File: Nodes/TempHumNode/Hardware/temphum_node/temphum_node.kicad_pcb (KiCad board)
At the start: 2 copper layers, 63.5 x 51.3 mm, 37 parts, among them IC1 CC1310F128RGZR, IC2 TPD6E004RSER, J1 TC2050-IDC, U1 MCP73123-22SI/MF, Y2 TSX-3225 24.0000MF15X-AC3, Y3 FC-135_32.7680KA-AG0

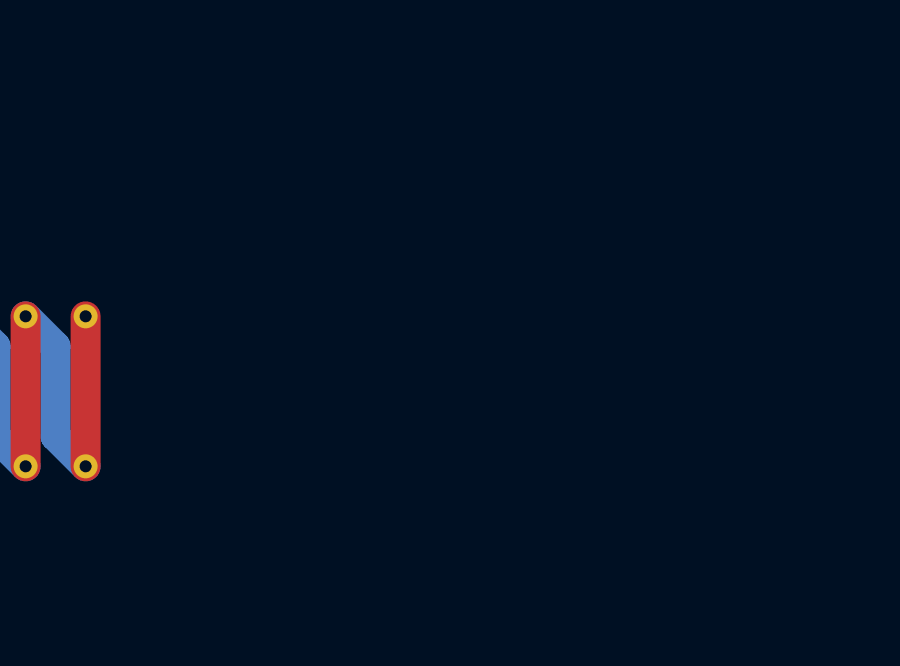
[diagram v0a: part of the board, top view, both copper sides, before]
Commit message: hw(temphum-node): add SHT35 (custom symbol layout) + schematic/board progress
Import SHT35-DIS-B (LCSC C90161) footprint + 3D model, and swap the
symbol graphics for the user's custom pin arrangement from the
temperatureSensorSubGHz project (keeps footprint link + LCSC/BOM
fields). Plus in-progress schematic/board work.

Co-Authored-By: Claude Opus 4.8 (1M context) <noreply@anthropic.com>
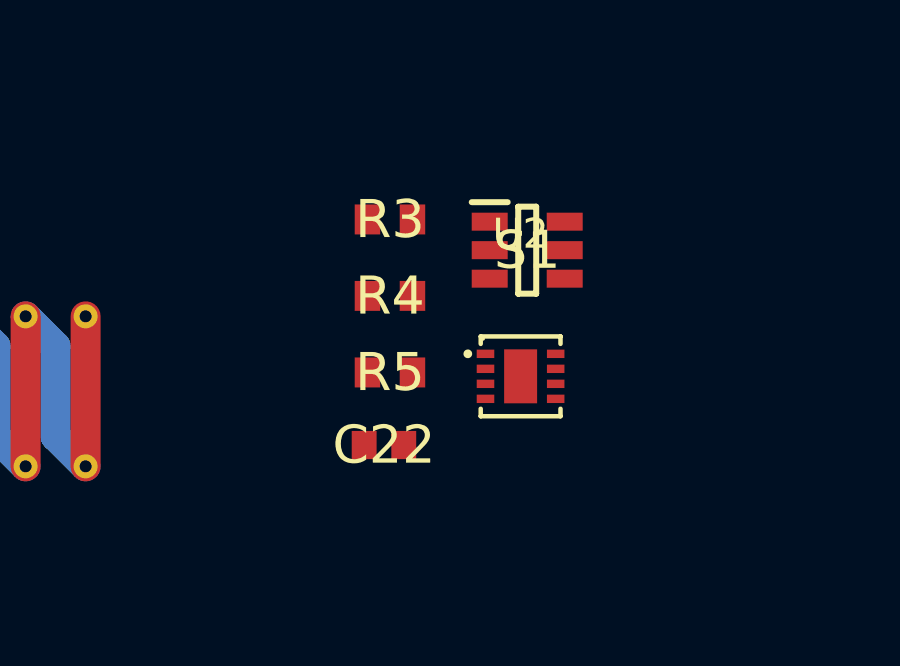
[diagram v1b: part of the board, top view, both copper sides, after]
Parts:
- added C22: 100nF, CC0603KRX7R9BB104:CAPC1608X90N, F.Cu at (179.3, 35.6)
- added R3: 10k, CRCW060310K0FKEA:RESC1608X50N, F.Cu at (179.5, 28.1)
- added R4: 10k, CRCW060310K0FKEA:RESC1608X50N, F.Cu at (179.5, 30.7)
- added R5: 10k, CRCW060310K0FKEA:RESC1608X50N, F.Cu at (179.5, 33.2)
- added S1: TPS22860DBVR, TPS22860DBVR:SOT95P280X145-6N, F.Cu at (184.1, 29.1)
- added U2: SHT35-DIS-B, SmartHome:DFN-8_L2.5-W2.5-P0.50-TL-EP, F.Cu at (183.9, 33.3)

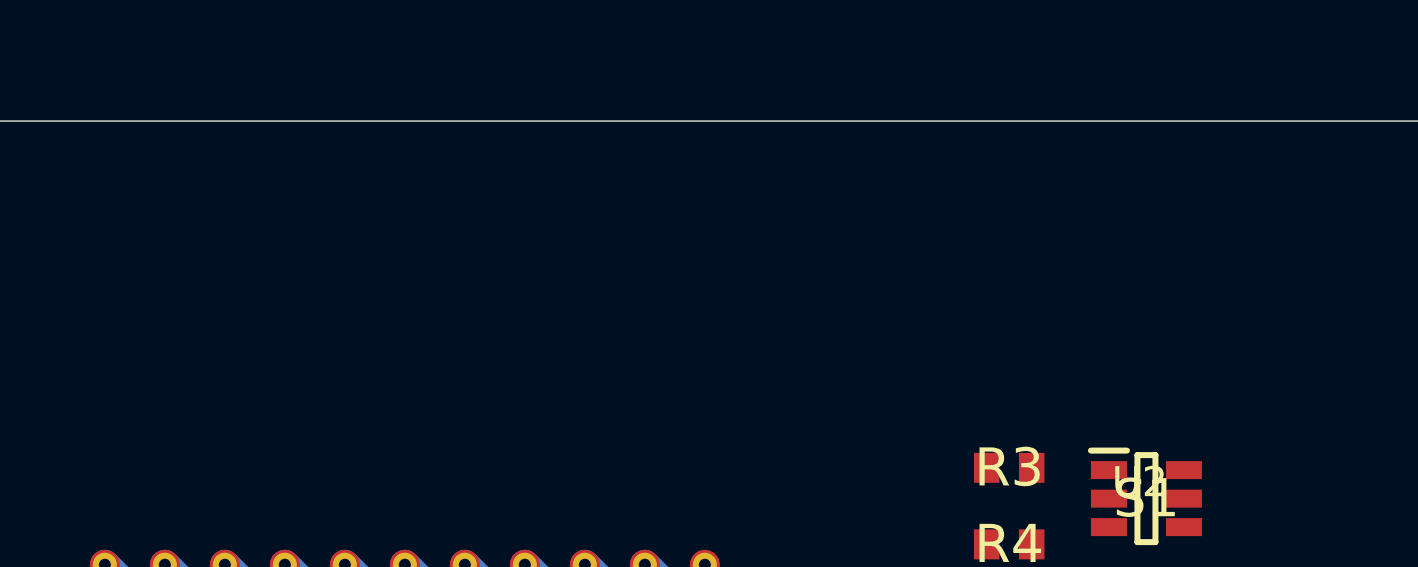
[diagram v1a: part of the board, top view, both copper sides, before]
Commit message: hw(temphum-node): add power/protection parts (TPS63900, MCP3421, TPS22860, PCM)
Import LDO/converter TPS63900 (buck-boost 3.3V), MCP3421A0 (18-bit ADC,
I2C 0x68 for battery SoC), TPS22860 (load switch), and the LiFePO4 PCM
pair HY2112 + FS8205A. Footprints/symbols/3D into Shared/KiCadLib.

Co-Authored-By: Claude Opus 4.8 (1M context) <noreply@anthropic.com>
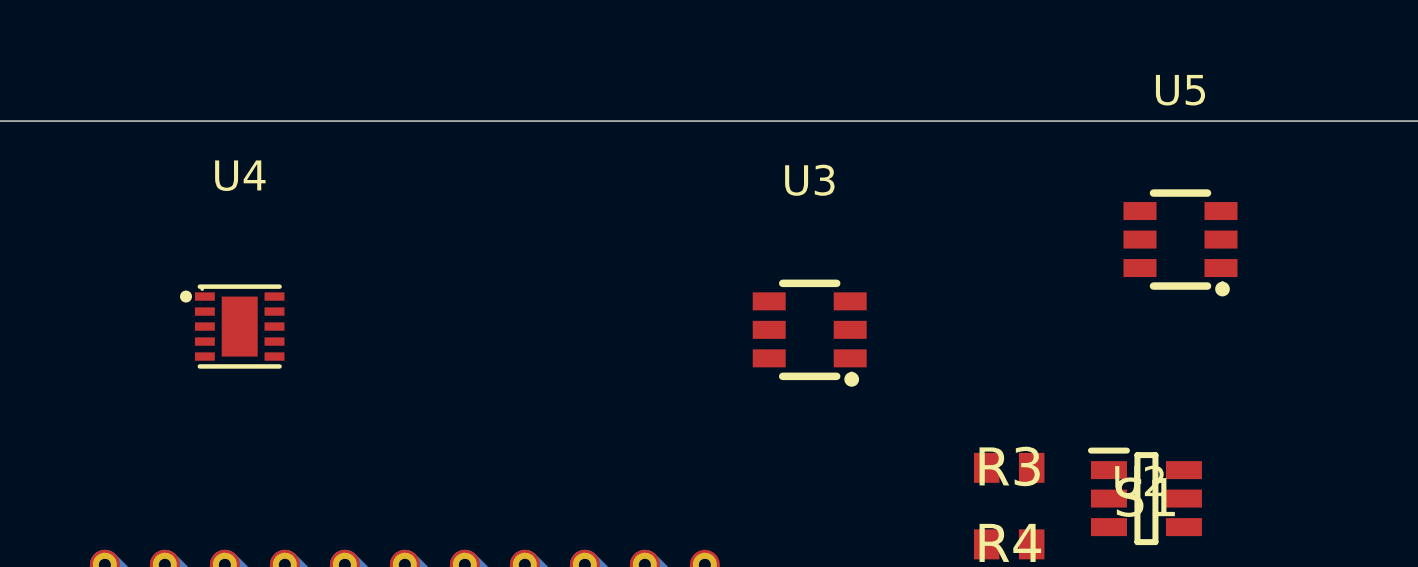
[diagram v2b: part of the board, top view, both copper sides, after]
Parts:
- added U3: TPS22860DBVR, SmartHome:SOT-23-6_L2.9-W1.6-P0.95-LS2.8-BR, F.Cu at (172.9, 23.5)
- added U4: TPS63900DSKR, SmartHome:WSON-10_L2.5-W2.5-W0.50-TL-EP, F.Cu at (153.9, 23.4)
- added U5: MCP3421A0T-E/CH, SmartHome:SOT-23-6_L2.9-W1.6-P0.95-LS2.8-BR, F.Cu at (185.2, 20.5)

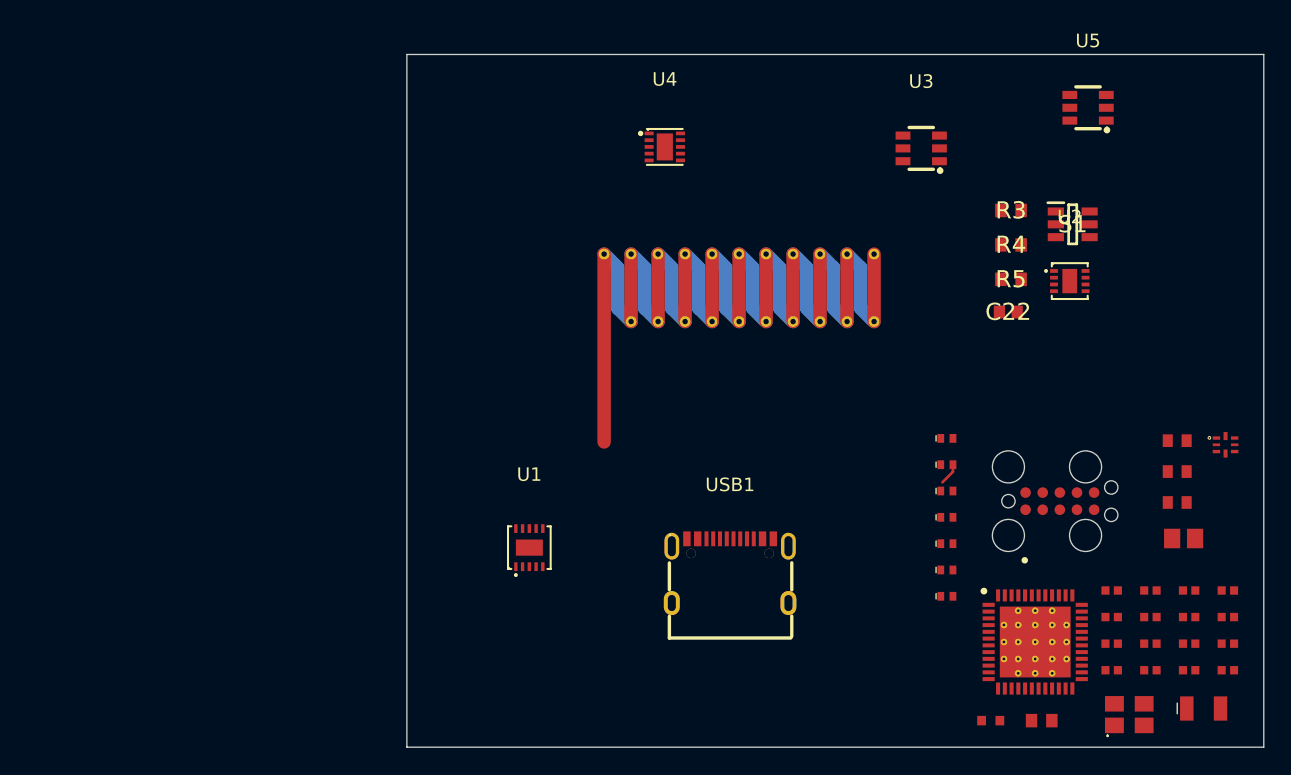
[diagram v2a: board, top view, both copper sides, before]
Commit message: hw(temphum-node): CC1310 support parts - pogo/ESD 3D, crystal swaps
Add TC2030-IDC UART pogo (SnapEDA, both footprints + 3D, symbol made
SmartHome-native). Attach TPD6E004 ESD 3D model + merge its symbol into
SmartHome. Add in-stock crystal replacements: ECS-240-9-33B (24MHz 9pF,
capless HF) and Epson FC-135R (32.768kHz 12.5pF, 2x12pF caps) - both CL/
ESR-matched drop-ins. Plus CC1310 schematic GPIO/pogo wiring.

Co-Authored-By: Claude Opus 4.8 (1M context) <noreply@anthropic.com>
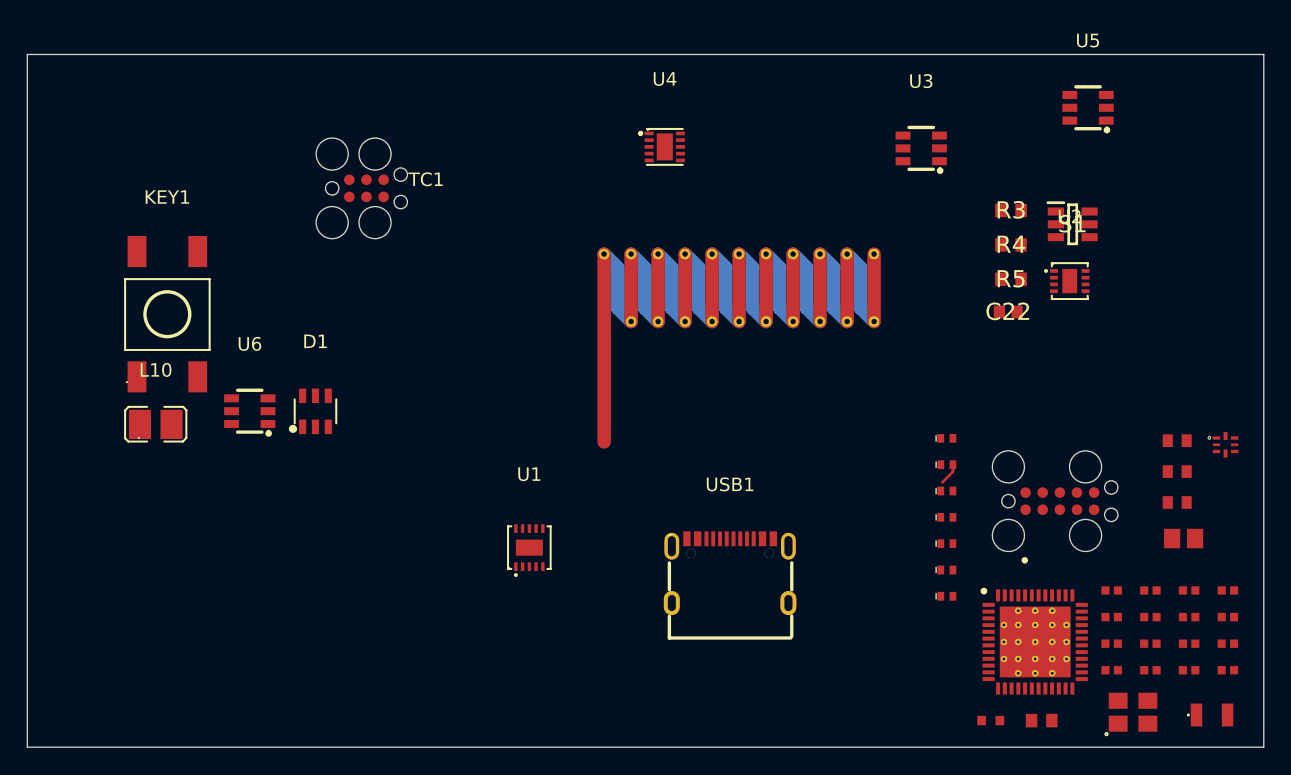
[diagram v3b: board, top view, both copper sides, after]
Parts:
- removed Y2: TSX-3225 24.0000MF15X-AC3, SmartHome:TSX3225240000MF15XAC3
- removed Y3: FC-135_32.7680KA-AG0, SmartHome:FC135327680KAAG0
- added D1: USBLC6-2SC6, SmartHome:SOT-23-6_L2.9-W1.6-P0.95-LS2.8-BL, F.Cu at (128.0, 43.0)
- added KEY1: TL3301AF160QG, SmartHome:KEY-SMD_4P-L6.0-W6.0-P4.50-LS10.0, F.Cu at (117.0, 35.8)
- added L10: DFE252012PD, SmartHome:L1008, F.Cu at (116.2, 44.0)
- added TC1: TC2030-IDC, SmartHome:TC2030-IDC, F.Cu at (131.8, 26.5)
- added U6: TPS22860DBVR, SmartHome:SOT-23-6_L2.9-W1.6-P0.95-LS2.8-BR, F.Cu at (123.1, 43.0)
- added U7: ECS-240-9-33B-CWN-TR, SmartHome:CRYSTAL-SMD_4P-L3.2-W2.5-BL, F.Cu at (188.6, 65.3)
- added X1: FC-135R, SmartHome:OSC-SMD_L3.2-W1.5, F.Cu at (194.4, 65.5)
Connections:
- C22 pad 1: VCC_SWITCH -> 3V3_SW
- IC1 pad 10: unconnected-(IC1-DIO_5-Pad10) -> PERIPH_EN
- IC1 pad 11: unconnected-(IC1-DIO_6-Pad11) -> nBUTTON
- IC1 pad 12: unconnected-(IC1-DIO_7-Pad12) -> nCHRGSTAT
- IC1 pad 37: LED_RED -> unconnected-(IC1-DIO_24-Pad37)
- IC1 pad 38: LED_BLUE -> unconnected-(IC1-DIO_25-Pad38)
- IC1 pad 39: TOUCH_OUT -> unconnected-(IC1-DIO_26-Pad39)
- IC1 pad 40: RELAY1 -> unconnected-(IC1-DIO_27-Pad40)
- IC1 pad 6: unconnected-(IC1-DIO_1-Pad6) -> SCL
- IC1 pad 7: unconnected-(IC1-DIO_2-Pad7) -> SDA
- IC1 pad 8: unconnected-(IC1-DIO_3-Pad8) -> UART_TX
- IC1 pad 9: unconnected-(IC1-DIO_4-Pad9) -> UART_RX
- IC2 pad 7: unconnected-(IC2-IO6-Pad7) -> nBUTTON
- R3 pad 2: VCC_SWITCH -> 3V3_SW
- R4 pad 2: VCC_SWITCH -> 3V3_SW
- R5 pad 2: VCC_SWITCH -> 3V3_SW
- U1 pad 1: unconnected-(U1-VDD-Pad1) -> VBUS
- U1 pad 10: unconnected-(U1-PROG-Pad10) -> Net-(U1-PROG)
- U1 pad 11: unconnected-(U1-EP-Pad11) -> GND
- U1 pad 2: unconnected-(U1-VDD-Pad2) -> VBUS
- U1 pad 3: unconnected-(U1-VBAT-Pad3) -> BAT+
- U1 pad 4: unconnected-(U1-VBAT-Pad4) -> BAT+
- U1 pad 7: unconnected-(U1-STAT-Pad7) -> nCHRGSTAT
- U1 pad 8: unconnected-(U1-VSS-Pad8) -> GND
- U1 pad 9: unconnected-(U1-VSS-Pad9) -> GND
- U2 pad 2: VCC_SWITCH -> 3V3_SW
- U2 pad 5: VCC_SWITCH -> 3V3_SW
- U3 pad 1: VCC_SWITCH -> 3V3_SW
- U3 pad 4: VCC -> 3V3
- U3 pad 5: VCC -> 3V3
- U3 pad 6: DRV_OUT -> PERIPH_EN
- U4 pad 1: unconnected-(U4-EN-Pad1) -> BAT+
- U4 pad 10: unconnected-(U4-VIN-Pad10) -> BAT+
- U4 pad 11: unconnected-(U4-EP-Pad11) -> GND
- U4 pad 2: unconnected-(U4-SEL-Pad2) -> BAT+
- U4 pad 3: unconnected-(U4-CFG1-Pad3) -> Net-(U4-CFG1)
- U4 pad 4: unconnected-(U4-CFG2-Pad4) -> GND
- U4 pad 5: unconnected-(U4-CFG3-Pad5) -> GND
- U4 pad 6: unconnected-(U4-VOUT-Pad6) -> 3V3
- U4 pad 7: unconnected-(U4-LX2-Pad7) -> Net-(U4-LX2)
- U4 pad 8: unconnected-(U4-GND-Pad8) -> GND
- U4 pad 9: unconnected-(U4-LX1-Pad9) -> Net-(U4-LX1)
- U5 pad 1: unconnected-(U5-Vin+-Pad1) -> Net-(U5-Vin+)
- U5 pad 2: unconnected-(U5-VSS-Pad2) -> GND
- U5 pad 3: unconnected-(U5-SCL-Pad3) -> SCL
- U5 pad 4: unconnected-(U5-SDA-Pad4) -> SDA
- U5 pad 5: unconnected-(U5-VDD-Pad5) -> 3V3_SW
- U5 pad 6: unconnected-(U5-Vin--Pad6) -> GND
- USB1 pad 13: unconnected-(USB1-EH-Pad13) -> GND
- USB1 pad 14: unconnected-(USB1-EH-Pad14) -> GND
- USB1 pad A1B12: unconnected-(USB1-GND-PadA1B12) -> GND
- USB1 pad A4B9: unconnected-(USB1-VBUS-PadA4B9) -> VBUS
- USB1 pad A5: unconnected-(USB1-CC1-PadA5) -> CC1
- USB1 pad B1A12: unconnected-(USB1-GND-PadB1A12) -> GND
- USB1 pad B4A9: unconnected-(USB1-VBUS-PadB4A9) -> VBUS
- USB1 pad B5: unconnected-(USB1-CC2-PadB5) -> CC2
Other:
- board size 63.5 x 51.3 mm -> 91.6 x 51.3 mm

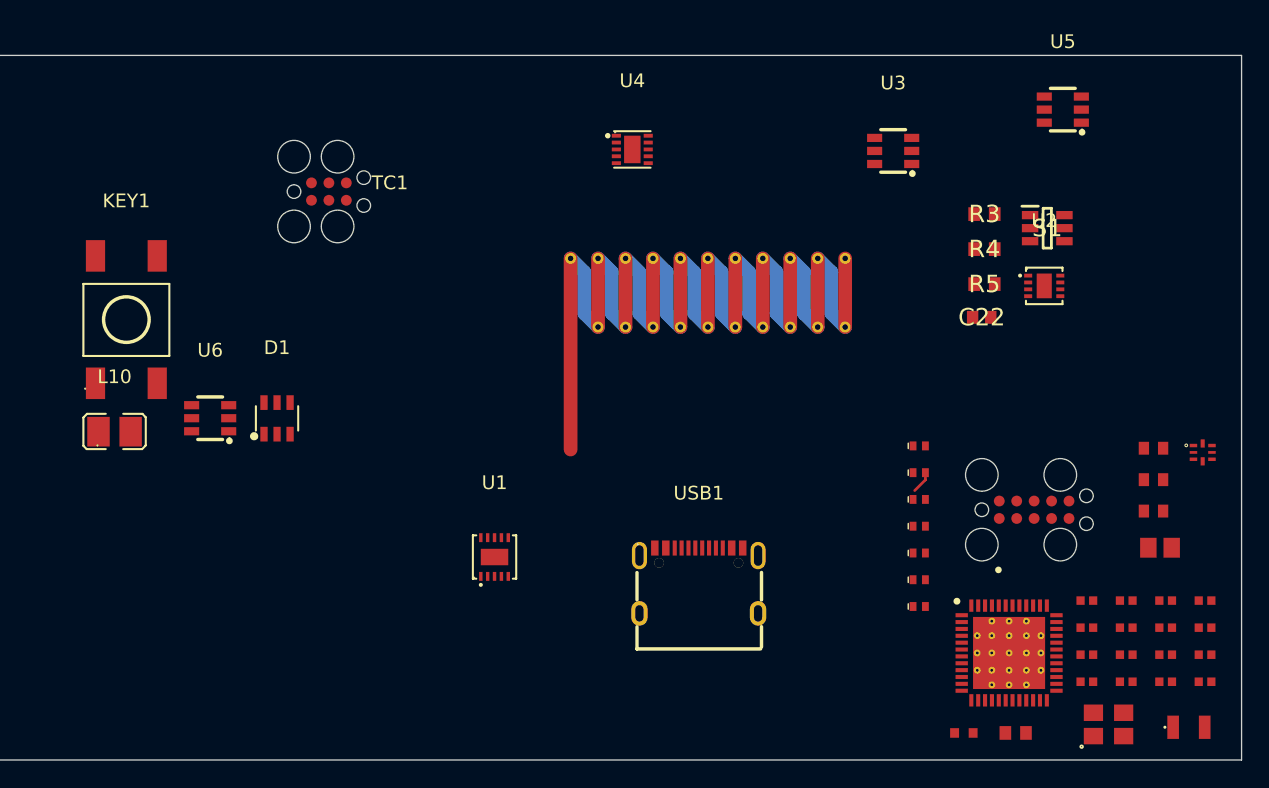
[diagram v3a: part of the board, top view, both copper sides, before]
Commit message: hw(temphum-node): passive footprints/3D, ferrite/inductor/LED/0805 parts
Add ferrite bead BLM18HE152 (L0603), DCDC inductor MLZ2012N6R8 (IND-
SMD), 0805 cap footprint, red LED XL-1608SURC (LED0603). Attach 3D
models to the perfected passive footprints (C_0402, C_0603, R_0603,
L_Polarized_0402) - library + all placed board instances; R_0603 model
orientation fixed (rotate 0 0 -90). Node schematic essentially
complete; only the battery connector remains before layout.

Co-Authored-By: Claude Opus 4.8 (1M context) <noreply@anthropic.com>
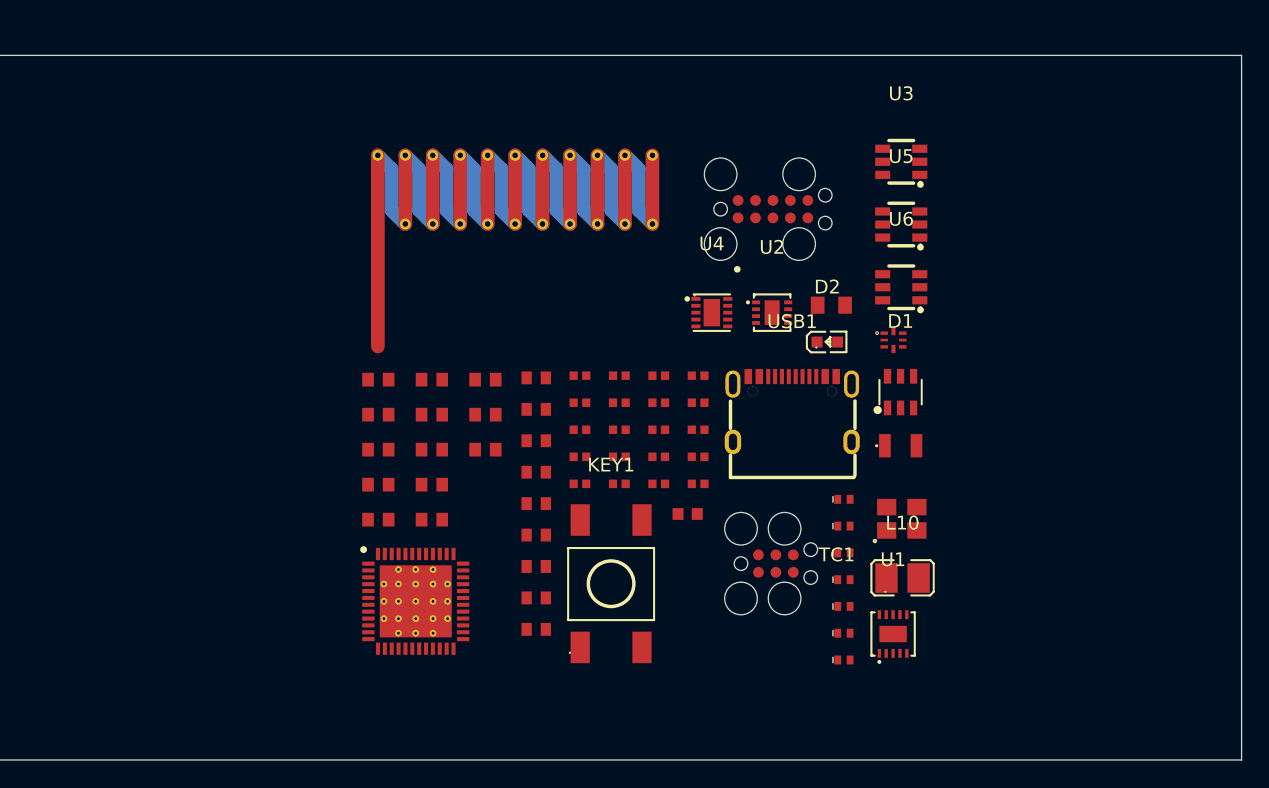
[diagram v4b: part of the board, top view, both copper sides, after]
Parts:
- removed L9: 6.8uH, SmartHome:MLZ2012N6R8LT000_0805
- removed S1: TPS22860DBVR, TPS22860DBVR:SOT95P280X145-6N
- added C1: 2.2nF, SmartHome:C_0603, F.Cu at (146.9, 40.0)
- added C2: 4.7uF, SmartHome:C_0603, F.Cu at (146.9, 42.3)
- added C23: 4.7uF, SmartHome:C_0603, F.Cu at (146.9, 51.5)
- added C24: 10uF, SmartHome:C_0603, F.Cu at (146.9, 53.8)
- added C26: 22uF, SmartHome:C_0603, F.Cu at (146.9, 58.4)
- added C27: 100nF, SmartHome:C_0402, F.Cu at (158.7, 43.8)
- added C28: 100nF, SmartHome:C_0402, F.Cu at (158.7, 45.8)
- added C29: 10nF, SmartHome:C_0402, F.Cu at (158.7, 47.8)
- added C3: 100nF, SmartHome:C_0402, F.Cu at (150.1, 39.9)
- added D2: RED, SmartHome:LED0603-RD_RED, F.Cu at (168.1, 37.4)
- added L11: MLZ2012N6R8LT000, SmartHome:IND-SMD_L2.0-W1.3, F.Cu at (168.4, 34.7)
- added R1: 47,5k, SmartHome:R_0603, F.Cu at (135.4, 40.2)
- added R10: 36.5k, SmartHome:R_0603, F.Cu at (139.3, 50.4)
- added R11: 1M 0.1%, SmartHome:R_0603, F.Cu at (143.2, 40.2)
- added R12: 1M 0.1%, SmartHome:R_0603, F.Cu at (143.2, 42.7)
- added R2: 5.1k, SmartHome:R_0603, F.Cu at (135.4, 42.7)
- added R6: 5.1k, SmartHome:R_0603, F.Cu at (139.3, 40.2)
- added R7: 3k, SmartHome:R_0603, F.Cu at (139.3, 42.7)
- added R8: 100k, SmartHome:R_0603, F.Cu at (139.3, 45.3)
- added R9: 1k, SmartHome:R_0603, F.Cu at (139.3, 47.8)
- C22: footprint CC0603KRX7R9BB104:CAPC1608X90N -> SmartHome:C_0603
- L8: footprint SmartHome:BLM18SP221SN1B -> SmartHome:L0603
- R3, R4, R5: footprint CRCW060310K0FKEA:RESC1608X50N -> SmartHome:R_0603
- moved L10 58.4 mm to (173.6, 54.6)
- moved U6 51.2 mm to (173.5, 33.4)
- moved R3 47.4 mm to (135.4, 45.3)
- moved R4 47.4 mm to (135.4, 47.8)
- moved R5 47.4 mm to (135.4, 50.4)
- moved D1 45.5 mm to (173.4, 41.1)
- moved C25 45.4 mm to (146.9, 56.1)
- moved C17 45.0 mm to (146.9, 44.6)
- moved C19 45.0 mm to (146.9, 46.9)
- moved R13 43.8 mm to (143.2, 45.3)
- moved IC1 43.4 mm to (138.1, 56.3)
- moved TC1 42.4 mm to (164.3, 53.6)
- moved C20 42.1 mm to (158.7, 39.9)
- moved C21 42.1 mm to (158.7, 41.8)
- moved C13 41.2 mm to (155.8, 39.9)
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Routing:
- net Net-(AE1-A): track 1.63 -> 0.00 mm
